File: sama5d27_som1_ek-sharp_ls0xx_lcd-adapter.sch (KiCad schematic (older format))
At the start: 10 parts, among them J1 XF2M-5015-1A, J2 1-1734592-0

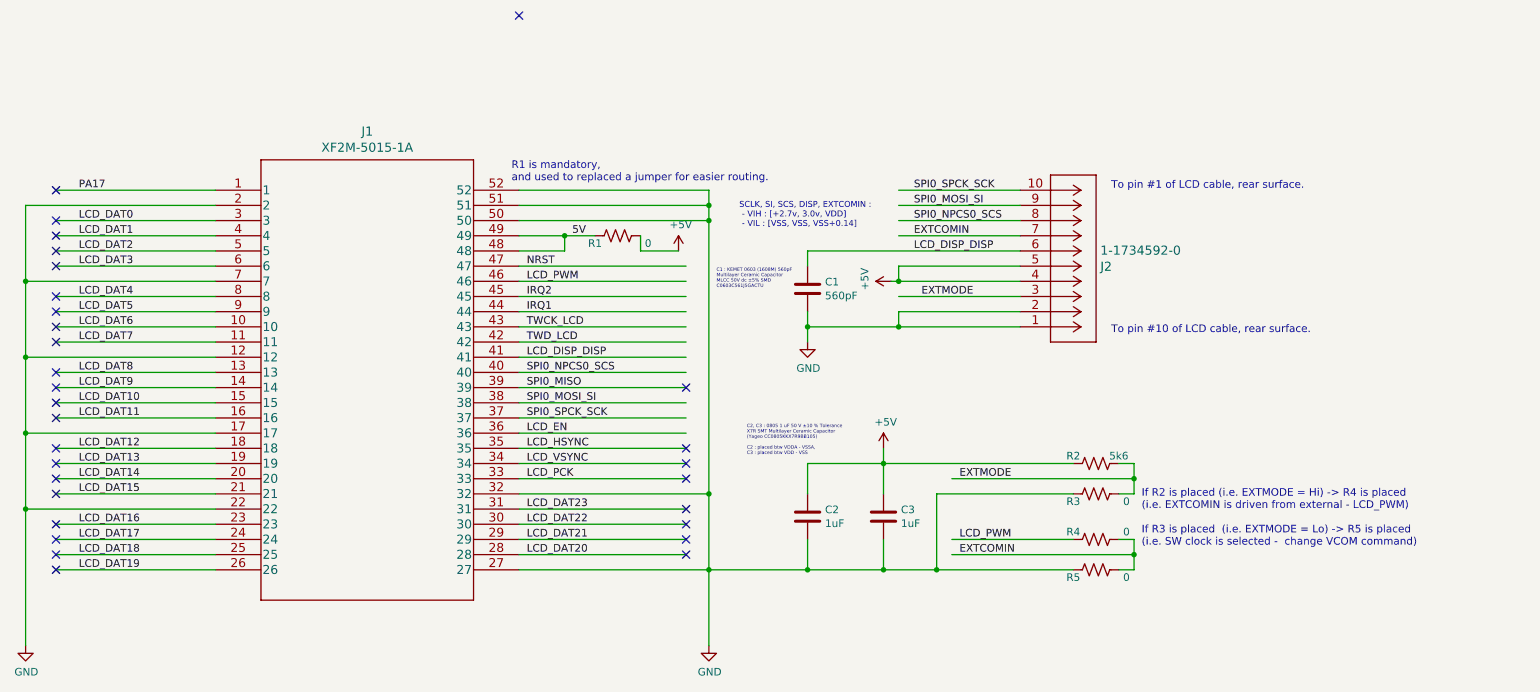
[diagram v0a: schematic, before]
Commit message: Pump to revision A1 (replacing J2)
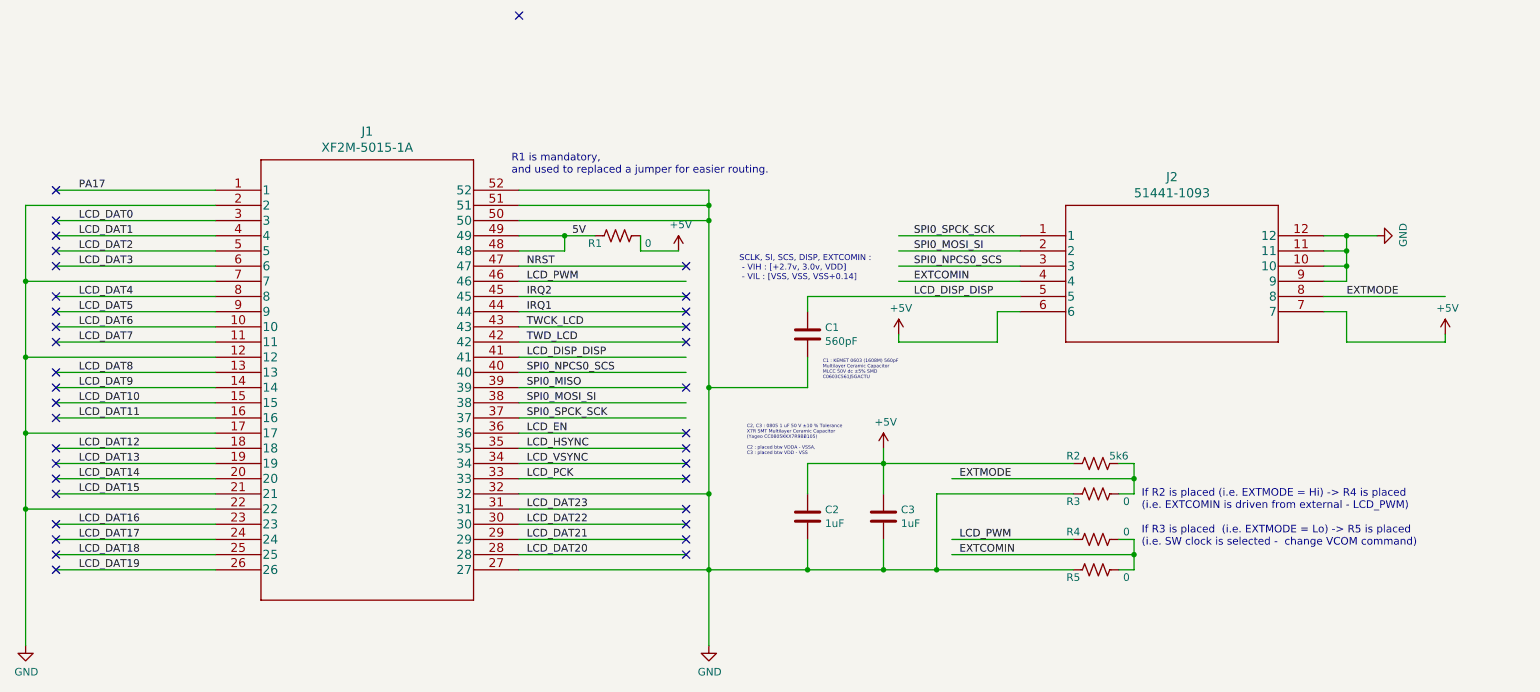
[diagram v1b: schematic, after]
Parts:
- removed J2: 1-1734592-0, footprints:1-1734592-0, symbol 1-1734592-0:1-1734592-0
- added J2: 51441-1093, footprints:51441-1093, symbol 51441-1093:51441-1093
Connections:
- wire segments 107 -> 116
- no-connect marks 30 -> 36
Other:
- note removed: "To pin #1 of LCD cable, rear surface."
- note removed: "To pin #10 of LCD cable, rear surface."
- moved on the sheet: C1
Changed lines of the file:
@@
 	1    0    0    -1
-$EndComp
-$Comp
-L 1-1734592-0:1-1734592-0 J2
-U 1 1 5FA444DA
-P 8050 2900
-F 0 "J2" H 8578 2503 60  0000 L CNN
-F 1 "1-1734592-0" H 8578 2397 60  0000 L CNN
-F 2 "footprints:1-1734592-0" H 8450 2440 60  0001 C CNN
-F 3 "" H 8050 2900 60  0000 C CNN
-	1    8050 2900
-	1    0    0    1
 $EndComp
 Wire Wire Line
@@
 	4750 4000 6000 4000
 Wire Wire Line
-	8050 2200 7250 2200
-Wire Wire Line
-	8050 2300 7250 2300
+	8050 2500 7250 2500
+Wire Wire Line
+	8050 2600 7250 2600
 Wire Wire Line
 	4750 2100 6000 2100
@@
 Text Label 1850 2300 0    50   ~ 0
 LCD_DAT1
-Text Label 7350 2000 0    50   ~ 0
+Text Label 7350 2300 0    50   ~ 0
 SPI0_SPCK_SCK
-Text Label 7350 2100 0    50   ~ 0
+Text Label 7350 2400 0    50   ~ 0
 SPI0_MOSI_SI
-Text Label 7350 2200 0    50   ~ 0
+Text Label 7350 2500 0    50   ~ 0
 SPI0_NPCS0_SCS
-Text Label 7350 2300 0    50   ~ 0
+Text Label 7350 2600 0    50   ~ 0
 EXTCOMIN
-Text Label 7350 2400 0    50   ~ 0
+Text Label 7350 2700 0    50   ~ 0
 LCD_DISP_DISP
 Wire Wire Line
-	8050 2700 7250 2700
-Text Label 7400 2700 0    50   ~ 0
+	10850 2700 10050 2700
+Text Label 10200 2700 0    50   ~ 0
 EXTMODE
-Wire Wire Line
-	7250 2600 7200 2600
 $Comp
 L power:+5V #PWR0104
@@
 L power:+5V #PWR0105
 U 1 1 5FB01D59
-P 7200 2600
-F 0 "#PWR0105" H 7200 2450 50  0001 C CNN
-F 1 "+5V" H 7215 2773 50  0000 C CNN
-F 2 "" H 7200 2600 50  0001 C CNN
-F 3 "" H 7200 2600 50  0001 C CNN
-	1    7200 2600
-	0    -1   -1   0
-$EndComp
-$Comp
-L Device:C C1
-U 1 1 5FB03613
-P 6650 2650
-F 0 "C1" H 6765 2696 50  0000 L CNN
-F 1 "560pF" H 6765 2605 50  0000 L CNN
-F 2 "Capacitor_SMD:C_0603_1608Metric" H 6688 2500 50  0001 C CNN
-F 3 "~" H 6650 2650 50  0001 C CNN
-	1    6650 2650
-	1    0    0    -1
-$EndComp
-Text Notes 6050 2650 0    22   ~ 0
-C1 : KEMET 0603 (1608M) 560pF \nMultilayer Ceramic Capacitor\nMLCC 50V dc ±5% SMD \nC0603C561J5GACTU
-Wire Wire Line
-	7250 2500 7250 2600
-Wire Wire Line
-	8050 2500 7250 2500
-Wire Wire Line
-	8050 2600 7250 2600
-Connection ~ 7250 2600
-Wire Wire Line
-	6650 2400 8050 2400
+P 7250 2950
+F 0 "#PWR0105" H 7250 2800 50  0001 C CNN
+F 1 "+5V" H 7265 3123 50  0000 C CNN
+F 2 "" H 7250 2950 50  0001 C CNN
+F 3 "" H 7250 2950 50  0001 C CNN
+	1    7250 2950
+	1    0    0    -1
+$EndComp
+Wire Wire Line
+	6650 2700 8050 2700
 NoConn ~ 1700 2300
 NoConn ~ 1700 2400
@@
 Wire Wire Line
 	7150 3800 7150 3700
-Wire Wire Line
-	7250 2800 7250 2900
-Wire Wire Line
-	7250 2800 8050 2800
-Wire Wire Line
-	7250 2900 8050 2900
 Text Label 1850 2200 0    50   ~ 0
 LCD_DAT0
@@
 	0    1    1    0
 $EndComp
-Wire Wire Line
-	6000 2200 6000 4000
 $Comp
 L Device:R_US R1
@@
 $EndComp
 $Comp
-L power:GND #PWR0103
-U 1 1 5FAE3964
-P 6650 3000
-F 0 "#PWR0103" H 6650 2750 50  0001 C CNN
-F 1 "GND" H 6655 2827 50  0000 C CNN
-F 2 "" H 6650 3000 50  0001 C CNN
-F 3 "" H 6650 3000 50  0001 C CNN
-	1    6650 3000
-	1    0    0    -1
-$EndComp
-Connection ~ 7250 2900
-Wire Wire Line
-	6650 3000 6650 2900
-Wire Wire Line
-	6650 2800 6650 2900
-Connection ~ 6650 2900
-Wire Wire Line
-	6650 2900 7250 2900
-$Comp
 L Device:R_US R3
 U 1 1 5FAB2BF0
@@
 $EndComp
 Wire Wire Line
-	6650 2400 6650 2500
-Wire Wire Line
 	6000 4500 6650 4500
 Wire Wire Line
@@
 	7150 3800 8400 3800
 Wire Wire Line
-	8050 2000 7250 2000
-Wire Wire Line
-	8050 2100 7250 2100
-Text Notes 8650 2950 0    50   ~ 0
-To pin #10 of LCD cable, rear surface.
-Text Notes 8650 2000 0    50   ~ 0
-To pin #1 of LCD cable, rear surface.
-Text Notes 4700 1950 0    50   ~ 0
+	8050 2300 7250 2300
+Wire Wire Line
+	8050 2400 7250 2400
+Text Notes 4700 1900 0    50   ~ 0
 R1 is mandatory, \nand used to replaced a jumper for easier routing.
 Text Notes 8850 4350 0    50   ~ 0
 If R2 is placed (i.e. EXTMODE = Hi) -> R4 is placed \n(i.e. EXTCOMIN is driven from external - LCD_PWM)\n\nIf R3 is placed  (i.e. EXTMODE = Lo) -> R5 is placed\n(i.e. SW clock is selected -  change VCOM command)
-Text Notes 6200 2250 0    39   ~ 0
+Text Notes 6200 2600 0    39   ~ 0
 SCLK, SI, SCS, DISP, EXTCOMIN :\n - VIH : [+2.7v, 3.0v, VDD]\n - VIL : [VSS, VSS, VSS+0.14]
 Text Label 5100 2300 0    50   ~ 0
 5V
+$Comp
+L power:GND #PWR0103
+U 1 1 5FAE3964
+P 10400 2300
+F 0 "#PWR0103" H 10400 2050 50  0001 C CNN
+F 1 "GND" H 10405 2127 50  0000 C CNN
+F 2 "" H 10400 2300 50  0001 C CNN
+F 3 "" H 10400 2300 50  0001 C CNN
+	1    10400 2300
+	0    -1   -1   0
+$EndComp
+Wire Wire Line
+	10400 2300 10200 2300
+$Comp
+L power:+5V #PWR0107
+U 1 1 5FB55A7B
+P 10850 2950
+F 0 "#PWR0107" H 10850 2800 50  0001 C CNN
+F 1 "+5V" H 10865 3123 50  0000 C CNN
+F 2 "" H 10850 2950 50  0001 C CNN
+F 3 "" H 10850 2950 50  0001 C CNN
+	1    10850 2950
+	1    0    0    -1
+$EndComp
+Wire Wire Line
+	10850 2950 10850 3000
+Wire Wire Line
+	10850 3000 10200 3000
+Wire Wire Line
+	10200 3000 10200 2800
+Wire Wire Line
+	10200 2800 10050 2800
+Wire Wire Line
+	7250 3000 7900 3000
+Wire Wire Line
+	7900 3000 7900 2800
+Wire Wire Line
+	7900 2800 8050 2800
+Wire Wire Line
+	7250 2950 7250 3000
+$Comp
+L 51441-1093:51441-1093 J2
+U 1 1 5FAA475B
+P 8050 2300
+F 0 "J2" H 9050 2687 60  0000 C CNN
+F 1 "51441-1093" H 9050 2581 60  0000 C CNN
+F 2 "footprints:51441-1093" H 9050 2540 60  0001 C CNN
+F 3 "" H 8050 2300 60  0000 C CNN
+	1    8050 2300
+	1    0    0    -1
+$EndComp
+Wire Wire Line
+	10050 2400 10200 2400
+Wire Wire Line
+	10200 2400 10200 2300
+Wire Wire Line
+	10050 2300 10200 2300
+Connection ~ 10200 2300
+Wire Wire Line
+	10050 2500 10200 2500
+Wire Wire Line
+	10200 2500 10200 2400
+Connection ~ 10200 2400
+Wire Wire Line
+	10050 2600 10200 2600
+Wire Wire Line
+	10200 2600 10200 2500
+Connection ~ 10200 2500
+Wire Wire Line
+	6650 2700 6650 2800
+Text Notes 6750 3250 0    22   ~ 0
+C1 : KEMET 0603 (1608M) 560pF \nMultilayer Ceramic Capacitor\nMLCC 50V dc ±5% SMD \nC0603C561J5GACTU
+$Comp
+L Device:C C1
+U 1 1 5FB03613
+P 6650 2950
+F 0 "C1" H 6765 2996 50  0000 L CNN
+F 1 "560pF" H 6765 2905 50  0000 L CNN
+F 2 "Capacitor_SMD:C_0603_1608Metric" H 6688 2800 50  0001 C CNN
+F 3 "~" H 6650 2950 50  0001 C CNN
+	1    6650 2950
+	1    0    0    -1
+$EndComp
+Wire Wire Line
+	6000 2200 6000 3300
+Wire Wire Line
+	6000 3300 6650 3300
+Wire Wire Line
+	6650 3300 6650 3100
+Connection ~ 6000 3300
+Wire Wire Line
+	6000 3300 6000 4000
+NoConn ~ 5850 2500
+NoConn ~ 5850 2700
+NoConn ~ 5850 2800
+NoConn ~ 5850 2900
+NoConn ~ 5850 3000
+NoConn ~ 5850 3600
 $EndSCHEMATC
